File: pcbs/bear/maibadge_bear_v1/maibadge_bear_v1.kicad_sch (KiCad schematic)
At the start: 13 parts, among them J1 Conn_01x04_Socket, SW1 SW_Push, SW2 SW_Push, SW3 SW_Push, SW4 SW_Push, U1 AMS1117-3.3, U2 ESP32-S3-WROOM-1

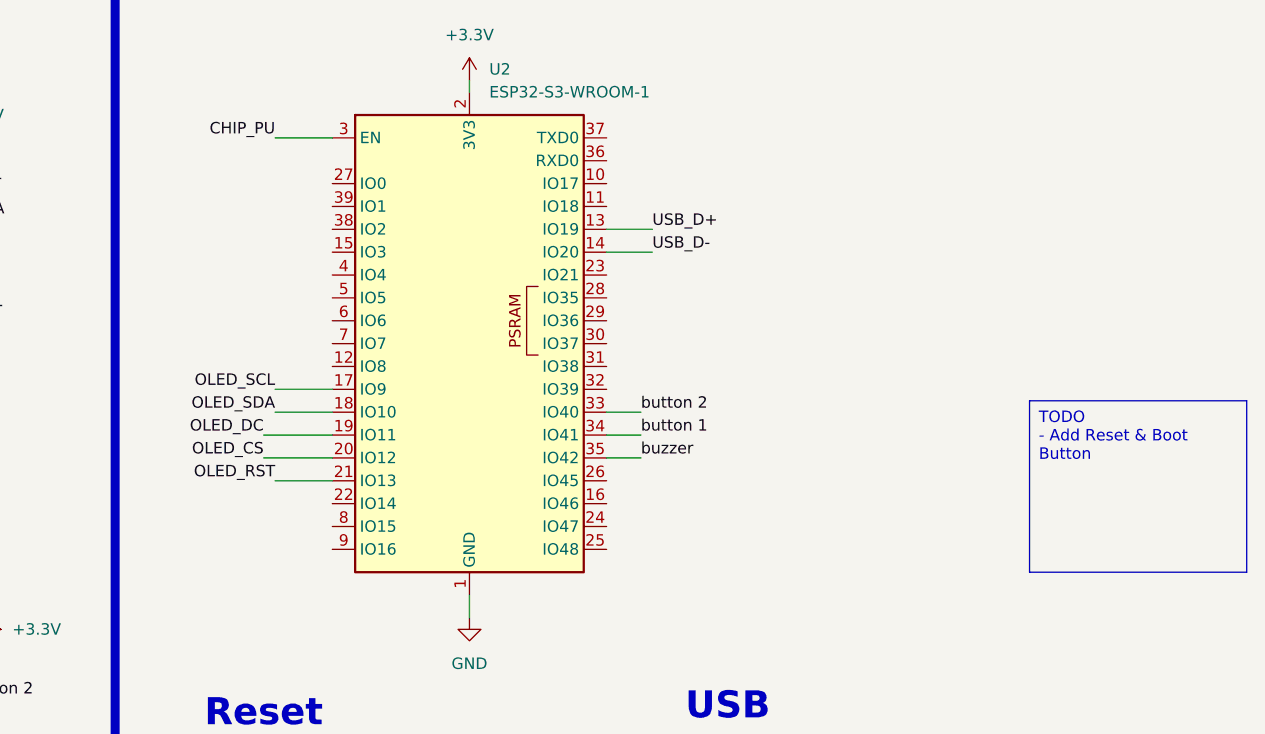
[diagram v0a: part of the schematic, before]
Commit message: feat: component placement adjustments
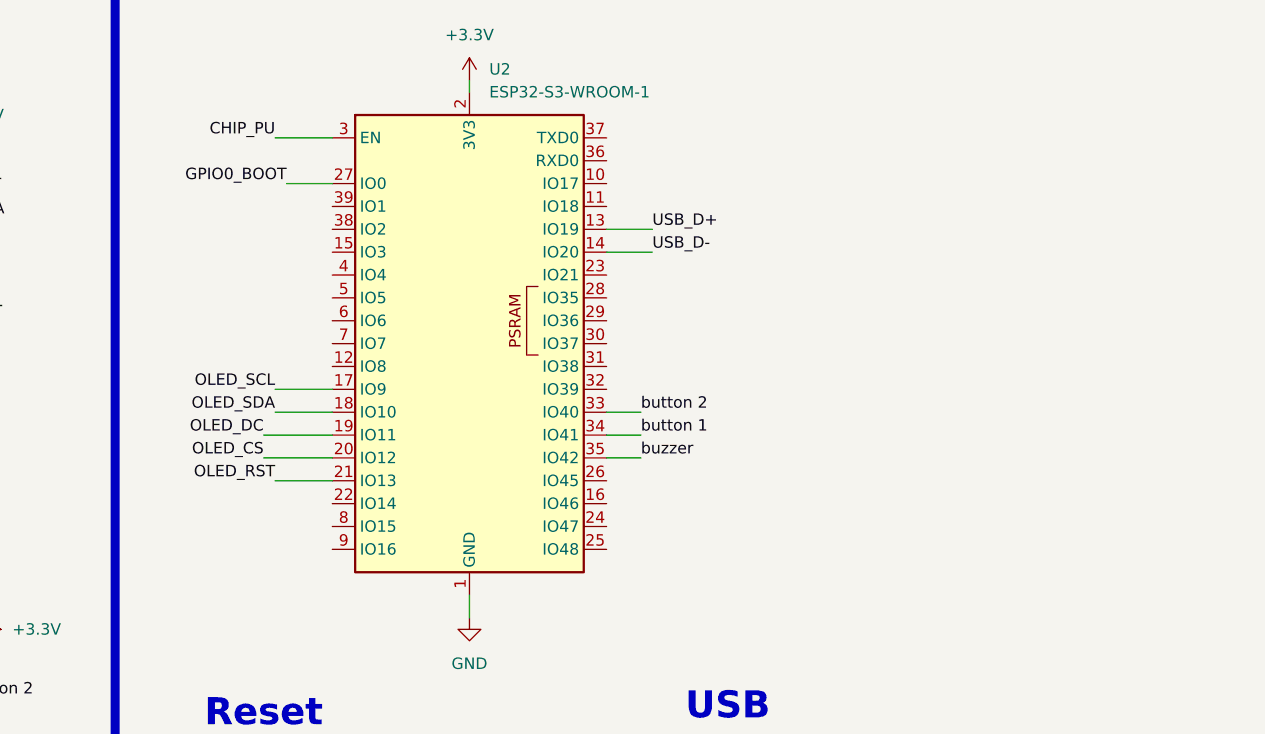
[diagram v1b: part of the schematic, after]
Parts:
- GC9A01: footprint Library:GC9A01 -> local_footprints:GC9A01
- J1: footprint Connector_PinHeader_1.00mm:PinHeader_1x04_P1.00mm_Vertical -> Connector_PinHeader_2.54mm:PinHeader_1x04_P2.54mm_Vertical
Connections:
- net GPIO0_BOOT: now also U2.27 (IO0)
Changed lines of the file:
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@@
+	(wire
+		(pts
+			(xy 88.9 43.18) (xy 93.98 43.18)
+		)
+		(stroke
+			(width 0)
+			(type default)
+		)
+	)
 	(wire
 		(pts
@@
 			(width 0)
 			(type default)
-		)
-	)
-	(text_box "TODO\n- Add Reset & Boot Button\n\n"
-		(exclude_from_sim no)
-		(at 171.45 67.31 0)
-		(size 24.13 19.05)
-		(stroke
-			(width 0)
-			(type default)
-		)
-		(fill
-			(type color)
-			(color 255 240 196 1)
-		)
-		(effects
-			(font
-				(size 1.27 1.27)
-			)
-			(justify left top)
 		)
 	)
@@
 	(label "CHIP_PU"
 		(at 110.49 121.92 180)
+		(fields_autoplaced yes)
+		(effects
+			(font
+				(size 1.27 1.27)
+			)
+			(justify right bottom)
+		)
+	)
+	(label "GPIO0_BOOT"
+		(at 88.9 43.18 180)
 		(fields_autoplaced yes)
 		(effects
@@
 			)
 		)
-		(property "Footprint" "Connector_PinHeader_1.00mm:PinHeader_1x04_P1.00mm_Vertical"
+		(property "Footprint" "Connector_PinHeader_2.54mm:PinHeader_1x04_P2.54mm_Vertical"
 			(at 154.94 115.57 0)
 			(effects
@@
 			)
 		)
-		(property "Footprint" "Library:GC9A01"
+		(property "Footprint" "local_footprints:GC9A01"
 			(at 31.75 46.99 0)
 			(effects

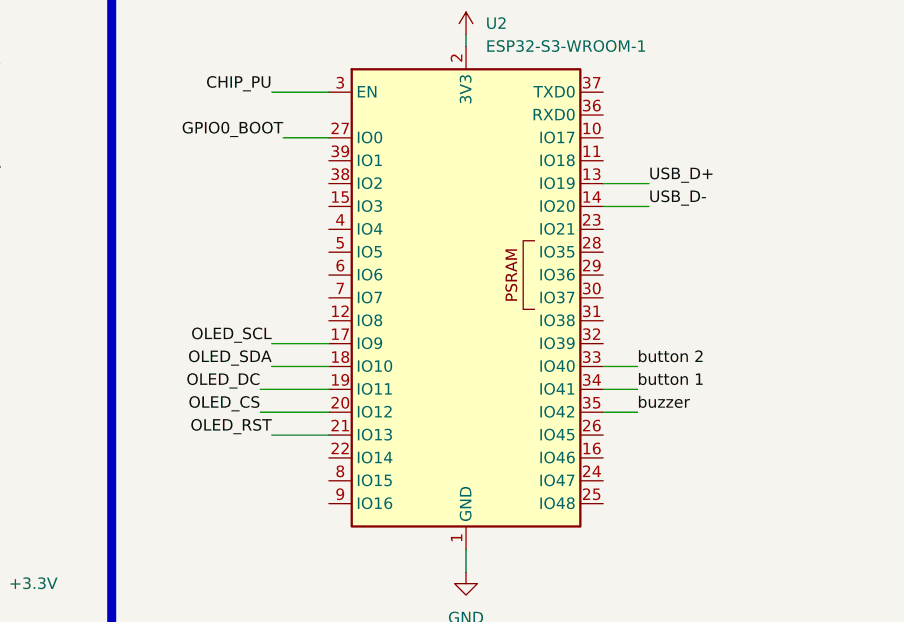
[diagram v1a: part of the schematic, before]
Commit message: changed OLED routing to HSPI, changed footprint for buttons and resistors, finished routing, ensured no components behind the 8 buttons
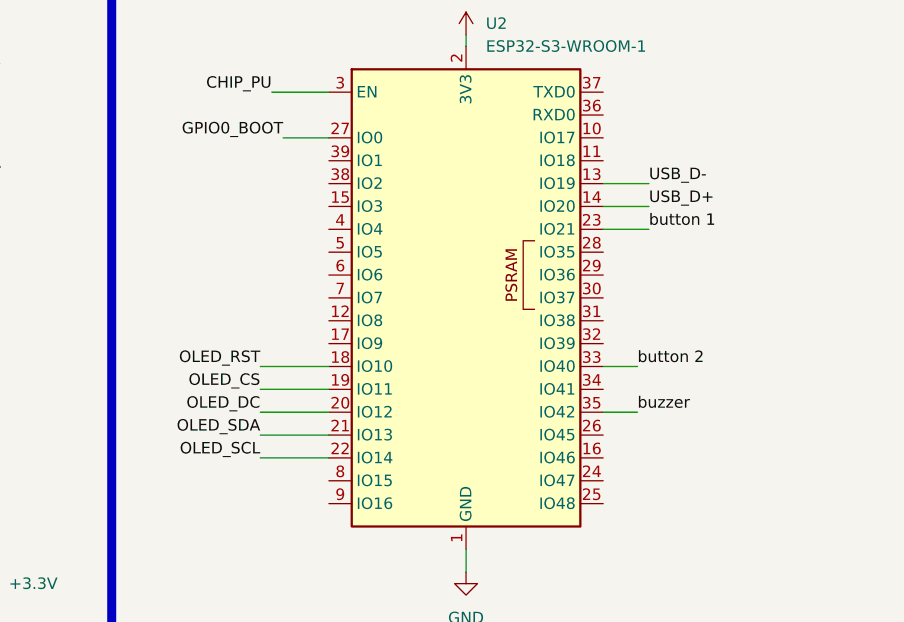
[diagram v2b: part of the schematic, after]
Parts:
- R1, R2, R3, R4: footprint Resistor_SMD:R_1206_3216Metric_Pad1.30x1.75mm_HandSolder -> Resistor_SMD:R_0805_2012Metric_Pad1.20x1.40mm_HandSolder
- SW1, SW2, SW3, SW4: footprint Button_Switch_SMD:SW_SPST_B3U-1000P -> Button_Switch_SMD:SW_Push_1P1T_XKB_TS-1187A
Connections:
- net OLED_CS: now also U2.19 (IO11); no longer U2.20 (IO12)
- net OLED_DC: now also U2.20 (IO12); no longer U2.19 (IO11)
- net OLED_RST: now also U2.18 (IO10); no longer U2.21 (IO13)
- net OLED_SCL: now also U2.22 (IO14); no longer U2.17 (IO9)
- net OLED_SDA: now also U2.21 (IO13); no longer U2.18 (IO10)
- net USB_D+: now also U2.14 (IO20); no longer U2.13 (IO19)
- net USB_D-: now also U2.13 (IO19); no longer U2.14 (IO20)
- net button 1: now also U2.23 (IO21); no longer U2.34 (IO41)
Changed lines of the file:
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@@
 	(wire
 		(pts
-			(xy 128.27 71.12) (xy 124.46 71.12)
-		)
-		(stroke
-			(width 0)
-			(type default)
-		)
-	)
-	(wire
-		(pts
-			(xy 129.54 48.26) (xy 124.46 48.26)
+			(xy 36.83 50.8) (xy 48.26 50.8)
+		)
+		(stroke
+			(width 0)
+			(type default)
+		)
+	)
+	(polyline
+		(pts
+			(xy 69.85 16.51) (xy 69.85 173.99)
+		)
+		(stroke
+			(width 1)
+			(type default)
+		)
+	)
+	(wire
+		(pts
+			(xy 86.36 71.12) (xy 93.98 71.12)
 		)
 		(stroke
@@
 	(wire
 		(pts
-			(xy 36.83 50.8) (xy 48.26 50.8)
-		)
-		(stroke
-			(width 0)
-			(type default)
-		)
-	)
-	(polyline
-		(pts
-			(xy 69.85 16.51) (xy 69.85 173.99)
-		)
-		(stroke
-			(width 1)
+			(xy 124.46 53.34) (xy 129.54 53.34)
+		)
+		(stroke
+			(width 0)
 			(type default)
 		)
@@
 	(wire
 		(pts
-			(xy 129.54 50.8) (xy 124.46 50.8)
-		)
-		(stroke
-			(width 0)
-			(type default)
-		)
-	)
-	(wire
-		(pts
 			(xy 138.43 113.03) (xy 149.86 113.03)
 		)
@@
 	(wire
 		(pts
-			(xy 87.63 68.58) (xy 93.98 68.58)
+			(xy 86.36 76.2) (xy 93.98 76.2)
 		)
 		(stroke
@@
 	(wire
 		(pts
+			(xy 86.36 78.74) (xy 93.98 78.74)
+		)
+		(stroke
+			(width 0)
+			(type default)
+		)
+	)
+	(wire
+		(pts
 			(xy 101.6 121.92) (xy 110.49 121.92)
 		)
@@
 	(wire
 		(pts
+			(xy 124.46 48.26) (xy 129.54 48.26)
+		)
+		(stroke
+			(width 0)
+			(type default)
+		)
+	)
+	(wire
+		(pts
 			(xy 87.63 38.1) (xy 93.98 38.1)
 		)
@@
 	(wire
 		(pts
+			(xy 86.36 68.58) (xy 93.98 68.58)
+		)
+		(stroke
+			(width 0)
+			(type default)
+		)
+	)
+	(wire
+		(pts
 			(xy 36.83 39.37) (xy 48.26 39.37)
 		)
@@
 	(wire
 		(pts
-			(xy 86.36 71.12) (xy 93.98 71.12)
-		)
-		(stroke
-			(width 0)
-			(type default)
-		)
-	)
-	(wire
-		(pts
-			(xy 87.63 66.04) (xy 93.98 66.04)
+			(xy 124.46 50.8) (xy 129.54 50.8)
 		)
 		(stroke
@@
 		(pts
 			(xy 88.9 43.18) (xy 93.98 43.18)
-		)
-		(stroke
-			(width 0)
-			(type default)
-		)
-	)
-	(wire
-		(pts
-			(xy 87.63 76.2) (xy 93.98 76.2)
 		)
 		(stroke
@@
 	)
 	(label "USB_D-"
-		(at 129.54 50.8 0)
+		(at 129.54 48.26 0)
 		(fields_autoplaced yes)
 		(effects
@@
 	)
 	(label "OLED_RST"
-		(at 87.63 76.2 180)
+		(at 86.36 68.58 180)
 		(fields_autoplaced yes)
 		(effects
@@
 		)
 	)
+	(label "button 1"
+		(at 129.54 53.34 0)
+		(fields_autoplaced yes)
+		(effects
+			(font
+				(size 1.27 1.27)
+			)
+			(justify left bottom)
+		)
+	)
 	(label "OLED_CS"
-		(at 86.36 73.66 180)
+		(at 86.36 71.12 180)
 		(fields_autoplaced yes)
 		(effects
@@
 	)
 	(label "OLED_SDA"
-		(at 87.63 68.58 180)
+		(at 86.36 76.2 180)
 		(fields_autoplaced yes)
 		(effects
@@
 	)
 	(label "USB_D+"
-		(at 129.54 48.26 0)
+		(at 129.54 50.8 0)
 		(fields_autoplaced yes)
 		(effects
@@
 		)
 	)
-	(label "button 1"
-		(at 128.27 71.12 0)
-		(fields_autoplaced yes)
-		(effects
-			(font
-				(size 1.27 1.27)
-			)
-			(justify left bottom)
-		)
-	)
 	(label "OLED_SCL"
-		(at 87.63 66.04 180)
+		(at 86.36 78.74 180)
 		(fields_autoplaced yes)
 		(effects
@@
 	)
 	(label "OLED_DC"
-		(at 86.36 71.12 180)
+		(at 86.36 73.66 180)
 		(fields_autoplaced yes)
 		(effects
@@
 			)
 		)
-		(property "Footprint" "Resistor_SMD:R_1206_3216Metric_Pad1.30x1.75mm_HandSolder"
+		(property "Footprint" "Resistor_SMD:R_0805_2012Metric_Pad1.20x1.40mm_HandSolder"
 			(at 105.41 113.792 90)
 			(effects
@@
 			)
 		)
-		(property "Footprint" "Button_Switch_SMD:SW_SPST_B3U-1000P"
+		(property "Footprint" "Button_Switch_SMD:SW_Push_1P1T_XKB_TS-1187A"
 			(at 96.52 134.62 0)
 			(effects
@@
 			)
 		)
-		(property "Footprint" "Resistor_SMD:R_1206_3216Metric_Pad1.30x1.75mm_HandSolder"
+		(property "Footprint" "Resistor_SMD:R_0805_2012Metric_Pad1.20x1.40mm_HandSolder"
 			(at 52.07 109.982 90)
 			(effects
@@
 			)
 		)
-		(property "Footprint" "Resistor_SMD:R_1206_3216Metric_Pad1.30x1.75mm_HandSolder"
+		(property "Footprint" "Resistor_SMD:R_0805_2012Metric_Pad1.20x1.40mm_HandSolder"
 			(at 50.8 90.932 90)
 			(effects
@@
 			)
 		)
-		(property "Footprint" "Button_Switch_SMD:SW_SPST_B3U-1000P"
+		(property "Footprint" "Button_Switch_SMD:SW_Push_1P1T_XKB_TS-1187A"
 			(at 41.91 87.63 0)
 			(effects
@@
 			)
 		)
-		(property "Footprint" "Resistor_SMD:R_1206_3216Metric_Pad1.30x1.75mm_HandSolder"
+		(property "Footprint" "Resistor_SMD:R_0805_2012Metric_Pad1.20x1.40mm_HandSolder"
 			(at 105.41 137.922 90)
 			(effects
@@
 			)
 		)
-		(property "Footprint" "Button_Switch_SMD:SW_SPST_B3U-1000P"
+		(property "Footprint" "Button_Switch_SMD:SW_Push_1P1T_XKB_TS-1187A"
 			(at 96.52 110.49 0)
 			(effects
@@
 			)
 		)
-		(property "Footprint" "Button_Switch_SMD:SW_SPST_B3U-1000P"
+		(property "Footprint" "Button_Switch_SMD:SW_Push_1P1T_XKB_TS-1187A"
 			(at 43.18 106.68 0)
 			(effects

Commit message: files for hardware
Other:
- note added: "LEDs"
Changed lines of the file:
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@@
+		)
+	)
+	(text "LEDs"
+		(exclude_from_sim no)
+		(at 178.562 20.066 0)
+		(effects
+			(font
+				(face "Consolas")
+				(size 4 4)
+				(thickness 0.8)
+				(bold yes)
+			)
 		)
 	)

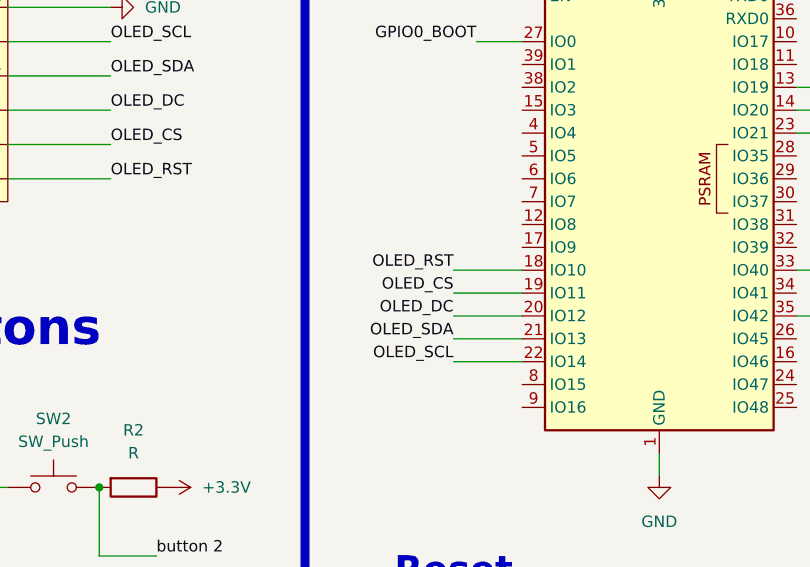
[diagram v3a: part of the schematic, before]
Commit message: pcb routing fixed
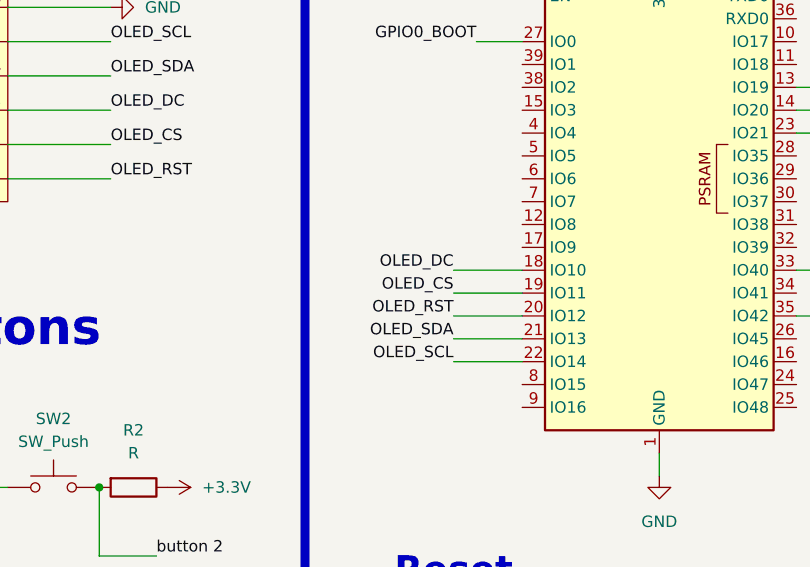
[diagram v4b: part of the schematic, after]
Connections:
- net OLED_DC: now also U2.18 (IO10); no longer U2.20 (IO12)
- net OLED_RST: now also U2.20 (IO12); no longer U2.18 (IO10)
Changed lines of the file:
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@@
+		)
+	)
+	(wire
+		(pts
+			(xy 86.36 68.58) (xy 93.98 68.58)
+		)
+		(stroke
+			(width 0)
+			(type default)
 		)
 	)
@@
 	(wire
 		(pts
+			(xy 124.46 53.34) (xy 129.54 53.34)
+		)
+		(stroke
+			(width 0)
+			(type default)
+		)
+	)
+	(wire
+		(pts
+			(xy 101.6 115.57) (xy 101.6 121.92)
+		)
+		(stroke
+			(width 0)
+			(type default)
+		)
+	)
+	(wire
+		(pts
+			(xy 46.99 92.71) (xy 46.99 100.33)
+		)
+		(stroke
+			(width 0)
+			(type default)
+		)
+	)
+	(wire
+		(pts
+			(xy 36.83 46.99) (xy 48.26 46.99)
+		)
+		(stroke
+			(width 0)
+			(type default)
+		)
+	)
+	(wire
+		(pts
+			(xy 33.02 111.76) (xy 38.1 111.76)
+		)
+		(stroke
+			(width 0)
+			(type default)
+		)
+	)
+	(wire
+		(pts
+			(xy 36.83 54.61) (xy 48.26 54.61)
+		)
+		(stroke
+			(width 0)
+			(type default)
+		)
+	)
+	(wire
+		(pts
+			(xy 36.83 43.18) (xy 48.26 43.18)
+		)
+		(stroke
+			(width 0)
+			(type default)
+		)
+	)
+	(wire
+		(pts
+			(xy 128.27 68.58) (xy 124.46 68.58)
+		)
+		(stroke
+			(width 0)
+			(type default)
+		)
+	)
+	(wire
+		(pts
+			(xy 109.22 91.44) (xy 109.22 88.9)
+		)
+		(stroke
+			(width 0)
+			(type default)
+		)
+	)
+	(wire
+		(pts
 			(xy 86.36 73.66) (xy 93.98 73.66)
 		)
@@
 	(wire
 		(pts
-			(xy 124.46 53.34) (xy 129.54 53.34)
-		)
-		(stroke
-			(width 0)
-			(type default)
-		)
-	)
-	(wire
-		(pts
-			(xy 101.6 115.57) (xy 101.6 121.92)
-		)
-		(stroke
-			(width 0)
-			(type default)
-		)
-	)
-	(wire
-		(pts
-			(xy 46.99 92.71) (xy 46.99 100.33)
-		)
-		(stroke
-			(width 0)
-			(type default)
-		)
-	)
-	(wire
-		(pts
-			(xy 36.83 46.99) (xy 48.26 46.99)
-		)
-		(stroke
-			(width 0)
-			(type default)
-		)
-	)
-	(wire
-		(pts
-			(xy 33.02 111.76) (xy 38.1 111.76)
-		)
-		(stroke
-			(width 0)
-			(type default)
-		)
-	)
-	(wire
-		(pts
-			(xy 36.83 54.61) (xy 48.26 54.61)
-		)
-		(stroke
-			(width 0)
-			(type default)
-		)
-	)
-	(wire
-		(pts
-			(xy 36.83 43.18) (xy 48.26 43.18)
-		)
-		(stroke
-			(width 0)
-			(type default)
-		)
-	)
-	(wire
-		(pts
-			(xy 128.27 68.58) (xy 124.46 68.58)
-		)
-		(stroke
-			(width 0)
-			(type default)
-		)
-	)
-	(wire
-		(pts
-			(xy 109.22 91.44) (xy 109.22 88.9)
-		)
-		(stroke
-			(width 0)
-			(type default)
-		)
-	)
-	(wire
-		(pts
 			(xy 138.43 115.57) (xy 149.86 115.57)
 		)
@@
 		(pts
 			(xy 87.63 38.1) (xy 93.98 38.1)
-		)
-		(stroke
-			(width 0)
-			(type default)
-		)
-	)
-	(wire
-		(pts
-			(xy 86.36 68.58) (xy 93.98 68.58)
 		)
 		(stroke
@@
 	)
 	(label "OLED_RST"
-		(at 86.36 68.58 180)
+		(at 86.36 73.66 180)
 		(fields_autoplaced yes)
 		(effects
@@
 	)
 	(label "OLED_DC"
-		(at 86.36 73.66 180)
-		(fields_autoplaced yes)
-		(effects
+		(at 86.36 68.58 180)
+		(fields_autoplaced yes)
+		(effects
